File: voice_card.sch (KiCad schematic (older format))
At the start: 207 parts, among them J1 PCI_11_49, Q1 MMBF4391LT1G, Q10 DMMT3906, Q11 BC857BS, Q2 2N3904, Q3 BCM847, Q4 DMMT3904, Q5 DMMT3906, Q6 MMBF4391LT1G, Q7 BCM847, Q8 2N3904, Q9 DMMT3904, U1 TL074-, U10 TL072-, U11 TL074-, U12 NE555, U13 LM311M, U14 CD4052, U15 TL072-, U16 TL072-, U17 LM13700, U18 LM13700, U19 LM13700, U2 TL074-, U20 TL072-, U3 NE555, U4 LF351, U5 TL072-, U6 LM311M, U7 CD4052, U8 TL074-, U9 LF351

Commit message: DDR3 DIMM schematic symbol created, now assigning ins and outs to DIMM pins. Tedious
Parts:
- removed J1: PCI_11_49, MyModules:PCI-49-11-CARD-EDGE, symbol PCI_11_49
- added J1: DDR3-DIMM, MyModules:DDR3-DIMM-MO-269, symbol DDR3-DIMM
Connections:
- wire segments 691 -> 891
- no-connect marks 8 -> 9

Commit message: DDR3 DIMM connector switched over from PCI in board and schematic. Routing power traces now
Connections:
- wire segments 891 -> 655
- no-connect marks 9 -> 19

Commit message: power routed, now stitching grounds
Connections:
- net +12V: now also J1.192, J1.210, J1.217, J1.238
- net -12V: now also J1.184, J1.197, J1.221
- net GND: now also J1.114, J1.116, J1.117, J1.119, J1.12, J1.127, J1.128, J1.129, J1.135, J1.14, J1.160, J1.177, J1.178, J1.179, J1.187, J1.188, J1.195, J1.203, J1.204, J1.228, J1.229, J1.239, J1.240
- no-connect marks 19 -> 14

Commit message: stitching ground plane
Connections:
- net GND: now also J1.102, J1.103, J1.151, J1.152, J1.219, J1.52, J1.53, J1.59, J1.66, J1.70
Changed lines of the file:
@@
+	1    0    0    -1
+$EndComp
+$Comp
+L GND_E #PWR0184
+U 1 1 5660624A
+P 4950 18800
+F 0 "#PWR0184" V 4950 18800 30  0001 C CNN
+F 1 "GND_E" H 4950 18730 30  0001 C CNN
+F 2 "" H 4950 18800 60  0000 C CNN
+F 3 "" H 4950 18800 60  0000 C CNN
+	1    4950 18800
+	1    0    0    -1
+$EndComp
+$Comp
+L GND_E #PWR0185
+U 1 1 5660A47B
+P 5675 30000
+F 0 "#PWR0185" V 5675 30000 30  0001 C CNN
+F 1 "GND_E" H 5675 29930 30  0001 C CNN
+F 2 "" H 5675 30000 60  0000 C CNN
+F 3 "" H 5675 30000 60  0000 C CNN
+	1    5675 30000
 	1    0    0    -1
 $EndComp
@@
 	36100 8075 35700 8075
 Wire Wire Line
-	35700 8075 35700 9550
+	35700 9550 35700 8075
 Wire Wire Line
 	36700 8850 36800 8850
@@
 	30800 9700 36100 9700
 Wire Wire Line
-	35700 9550 35250 9550
+	35250 9550 35700 9550
 Wire Wire Line
 	35550 7750 35550 8575
@@
 	32450 5650 32600 5650
 Wire Wire Line
-	32600 5650 32600 4450
-Wire Wire Line
-	32600 4450 29700 4450
+	32600 4450 32600 5650
+Wire Wire Line
+	29700 4450 32600 4450
 Wire Wire Line
 	29700 4450 29700 4500
@@
 	35700 16875 35300 16875
 Wire Wire Line
-	35300 16875 35300 17375
+	35300 17375 35300 16875
 Wire Wire Line
 	36300 17275 36400 17275
@@
 	30400 17875 35700 17875
 Wire Wire Line
-	35300 17375 34850 17375
+	34850 17375 35300 17375
 Wire Wire Line
 	35150 15550 35150 16325
@@
 	32050 13450 32200 13450
 Wire Wire Line
-	32200 13450 32200 12250
-Wire Wire Line
-	32200 12250 29300 12250
+	32200 12250 32200 13450
+Wire Wire Line
+	29300 12250 32200 12250
 Wire Wire Line
 	29300 12250 29300 12300
@@
 	4550 23750 5675 23750
 Connection ~ 5675 23750
+Wire Wire Line
+	4950 18550 4950 18800
+Wire Wire Line
+	4950 18550 4550 18550
+Wire Wire Line
+	4550 18650 4950 18650
+Connection ~ 4950 18650
+Wire Wire Line
+	4550 18750 4950 18750
+Connection ~ 4950 18750
+Wire Wire Line
+	5675 29750 5675 30000
+Wire Wire Line
+	5675 29750 4550 29750
+Wire Wire Line
+	4550 29850 5675 29850
+Connection ~ 5675 29850
+Wire Wire Line
+	3075 29750 3950 29750
+Connection ~ 3075 29550
 $Comp
-L GND_E #PWR0184
-U 1 1 5660624A
-P 4950 18800
-F 0 "#PWR0184" V 4950 18800 30  0001 C CNN
-F 1 "GND_E" H 4950 18730 30  0001 C CNN
-F 2 "" H 4950 18800 60  0000 C CNN
-F 3 "" H 4950 18800 60  0000 C CNN
-	1    4950 18800
+L GND_E #PWR0186
+U 1 1 5660CF32
+P 2825 28300
+F 0 "#PWR0186" V 2825 28300 30  0001 C CNN
+F 1 "GND_E" H 2825 28230 30  0001 C CNN
+F 2 "" H 2825 28300 60  0000 C CNN
+F 3 "" H 2825 28300 60  0000 C CNN
+	1    2825 28300
+	-1   0    0    -1
+$EndComp
+Wire Wire Line
+	2825 28050 2825 28300
+$Comp
+L GND_E #PWR0187
+U 1 1 5660D926
+P 2825 24700
+F 0 "#PWR0187" V 2825 24700 30  0001 C CNN
+F 1 "GND_E" H 2825 24630 30  0001 C CNN
+F 2 "" H 2825 24700 60  0000 C CNN
+F 3 "" H 2825 24700 60  0000 C CNN
+	1    2825 24700
+	-1   0    0    -1
+$EndComp
+Wire Wire Line
+	2825 24450 2825 24700
+Wire Wire Line
+	2825 24450 3950 24450
+$Comp
+L GND_E #PWR0188
+U 1 1 5660E6B9
+P 2825 24000
+F 0 "#PWR0188" V 2825 24000 30  0001 C CNN
+F 1 "GND_E" H 2825 23930 30  0001 C CNN
+F 2 "" H 2825 24000 60  0000 C CNN
+F 3 "" H 2825 24000 60  0000 C CNN
+	1    2825 24000
+	-1   0    0    -1
+$EndComp
+Wire Wire Line
+	2825 23750 2825 24000
+Wire Wire Line
+	2825 23750 3950 23750
+$Comp
+L GND_E #PWR0189
+U 1 1 5660EC2D
+P 2825 25100
+F 0 "#PWR0189" V 2825 25100 30  0001 C CNN
+F 1 "GND_E" H 2825 25030 30  0001 C CNN
+F 2 "" H 2825 25100 60  0000 C CNN
+F 3 "" H 2825 25100 60  0000 C CNN
+	1    2825 25100
+	-1   0    0    -1
+$EndComp
+Wire Wire Line
+	2825 24850 2825 25100
+Wire Wire Line
+	2825 24850 3950 24850
+Wire Wire Line
+	2825 23050 3950 23050
+Wire Wire Line
+	3950 23150 2825 23150
+Connection ~ 2825 23150
+$Comp
+L GND_E #PWR0190
+U 1 1 5660FCD3
+P 2825 23300
+F 0 "#PWR0190" V 2825 23300 30  0001 C CNN
+F 1 "GND_E" H 2825 23230 30  0001 C CNN
+F 2 "" H 2825 23300 60  0000 C CNN
+F 3 "" H 2825 23300 60  0000 C CNN
+	1    2825 23300
+	-1   0    0    -1
+$EndComp
+Wire Wire Line
+	2825 23050 2825 23300
+Wire Wire Line
+	5050 20950 4550 20950
+Wire Wire Line
+	4550 21050 5050 21050
+Connection ~ 5050 21050
+$Comp
+L GND_E #PWR0191
+U 1 1 566108F5
+P 5050 21200
+F 0 "#PWR0191" V 5050 21200 30  0001 C CNN
+F 1 "GND_E" H 5050 21130 30  0001 C CNN
+F 2 "" H 5050 21200 60  0000 C CNN
+F 3 "" H 5050 21200 60  0000 C CNN
+	1    5050 21200
 	1    0    0    -1
 $EndComp
 Wire Wire Line
-	4950 18550 4950 18800
-Wire Wire Line
-	4950 18550 4550 18550
-Wire Wire Line
-	4550 18650 4950 18650
-Connection ~ 4950 18650
-Wire Wire Line
-	4550 18750 4950 18750
-Connection ~ 4950 18750
+	5050 20950 5050 21200
 $Comp
 L GND_E #PWR?
-U 1 1 5660A47B
-P 5675 30000
-F 0 "#PWR?" V 5675 30000 30  0001 C CNN
-F 1 "GND_E" H 5675 29930 30  0001 C CNN
-F 2 "" H 5675 30000 60  0000 C CNN
-F 3 "" H 5675 30000 60  0000 C CNN
-	1    5675 30000
+U 1 1 5661486B
+P 5675 28000
+F 0 "#PWR?" V 5675 28000 30  0001 C CNN
+F 1 "GND_E" H 5675 27930 30  0001 C CNN
+F 2 "" H 5675 28000 60  0000 C CNN
+F 3 "" H 5675 28000 60  0000 C CNN
+	1    5675 28000
 	1    0    0    -1
 $EndComp
 Wire Wire Line
-	5675 29750 5675 30000
-Wire Wire Line
-	5675 29750 4550 29750
-Wire Wire Line
-	4550 29850 5675 29850
-Connection ~ 5675 29850
-Wire Wire Line
-	3075 29750 3950 29750
-Connection ~ 3075 29550
+	5675 27750 5675 28000
+Wire Wire Line
+	5675 27750 4550 27750
 $EndSCHEMATC

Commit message: decoupling caps placed and routed. Still stitching ground plane
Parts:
- added C35, C36, C37, C38, C39, C40: 100n, MyModules:SM0603-C-JRL, symbol C_US
- TP1, TP8: footprint MyModules:TEST_POINT_5000_SERIES -> MyModules:TEST_PAD
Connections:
- net +12V: now also C35.1, C37.1, C39.1
- net -12V: now also C36.2, C38.2, C40.2
- net GND: now also J1.164, J1.78, C35.2, C36.1, C37.2, C38.1, C39.2, C40.1

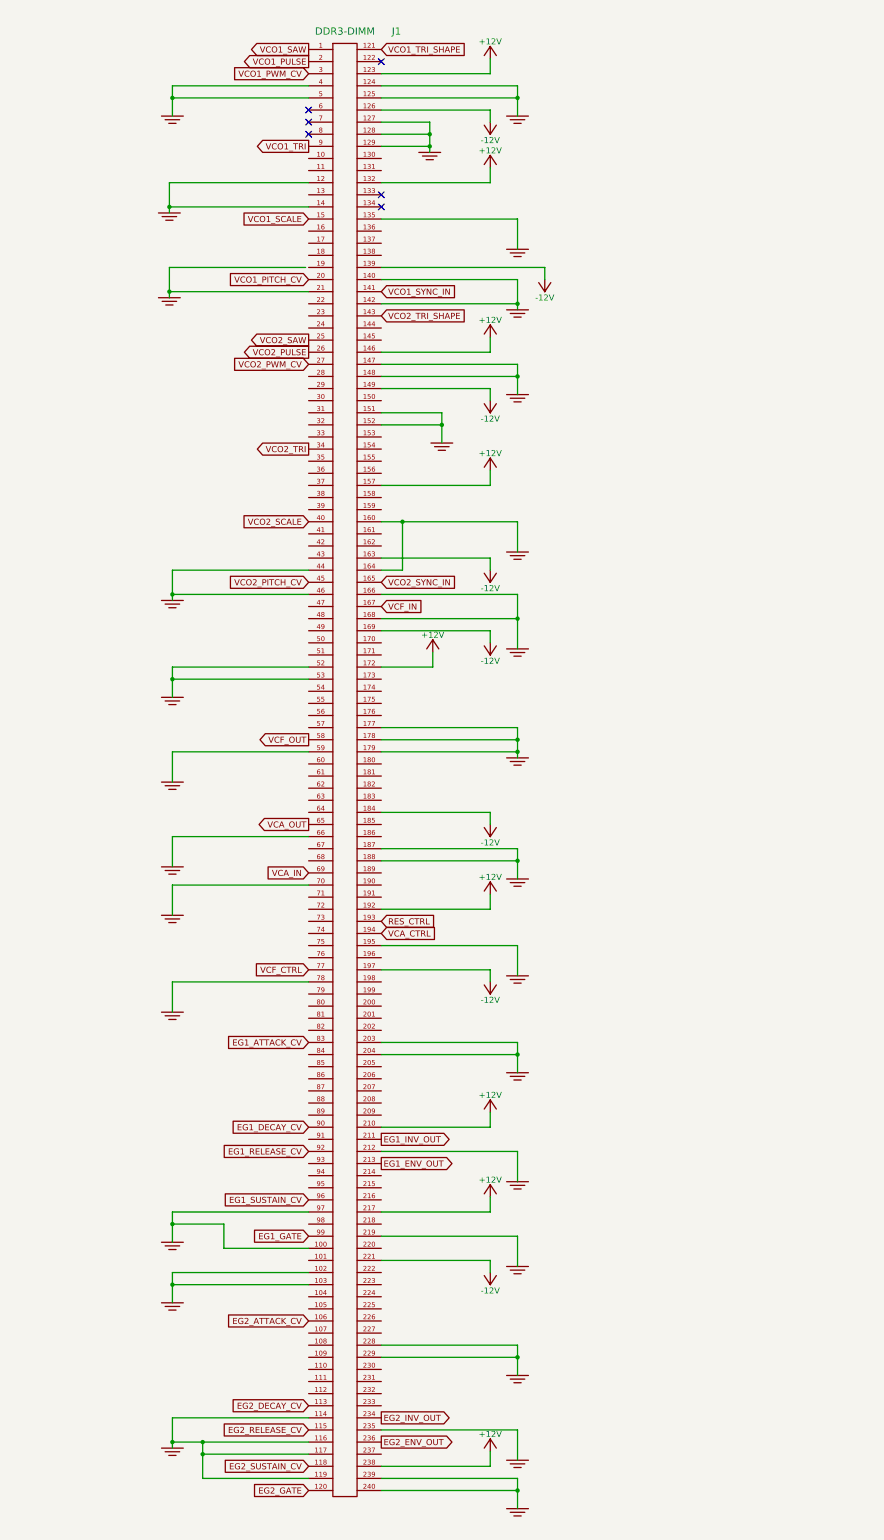
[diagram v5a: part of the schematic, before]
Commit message: placed silkscreen component references. still need to finish up ground stitching
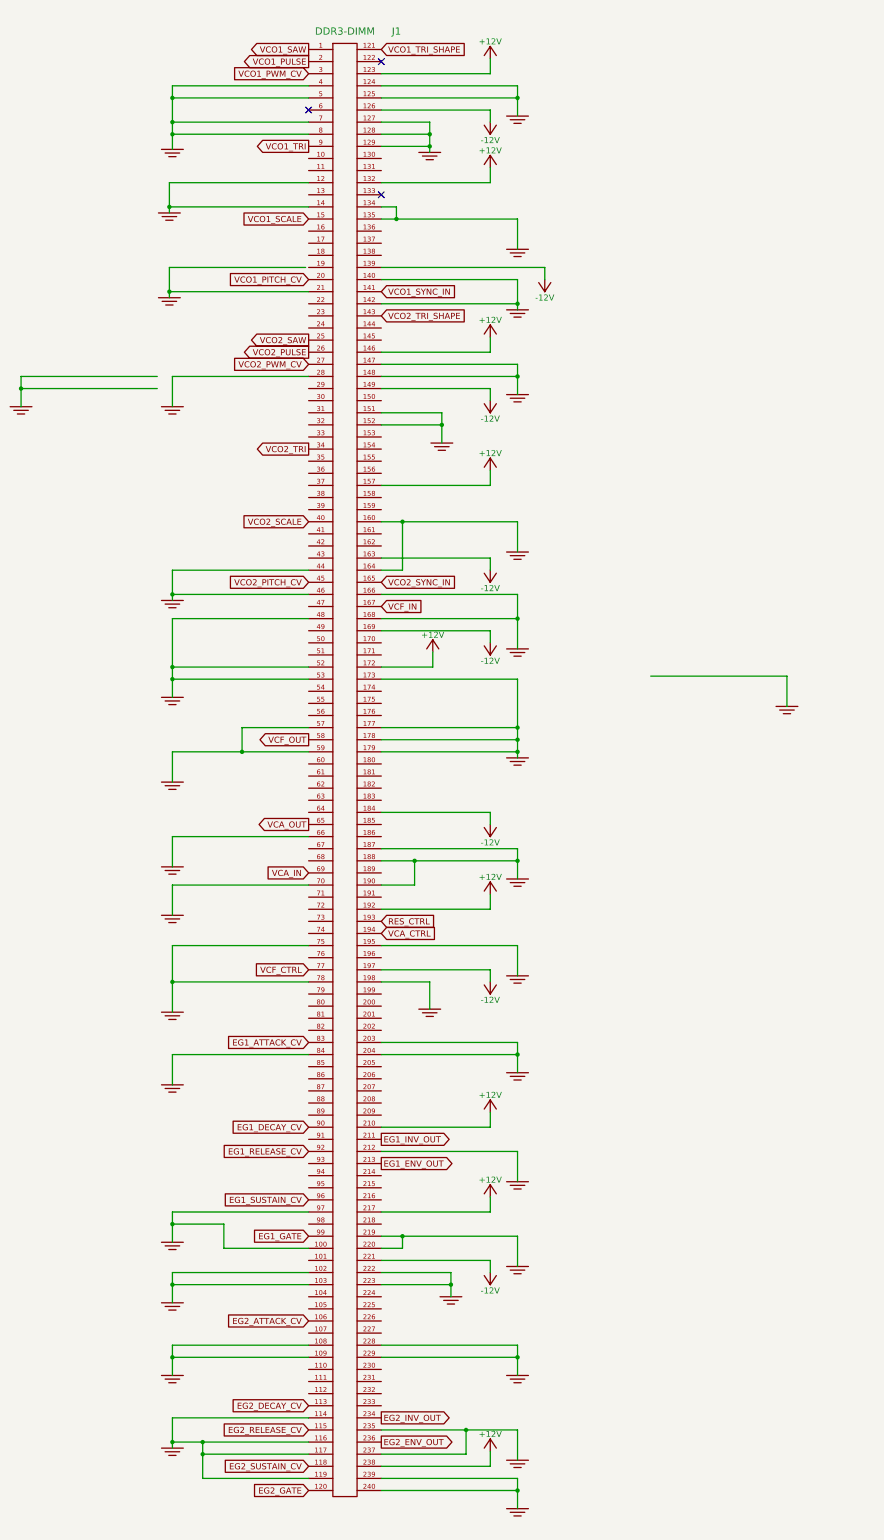
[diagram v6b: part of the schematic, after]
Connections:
- net GND: now also J1.108, J1.109, J1.134, J1.173, J1.190, J1.198, J1.220, J1.222, J1.223, J1.237, J1.28, J1.48, J1.57, J1.7, J1.75, J1.8, J1.84
- no-connect marks 14 -> 11

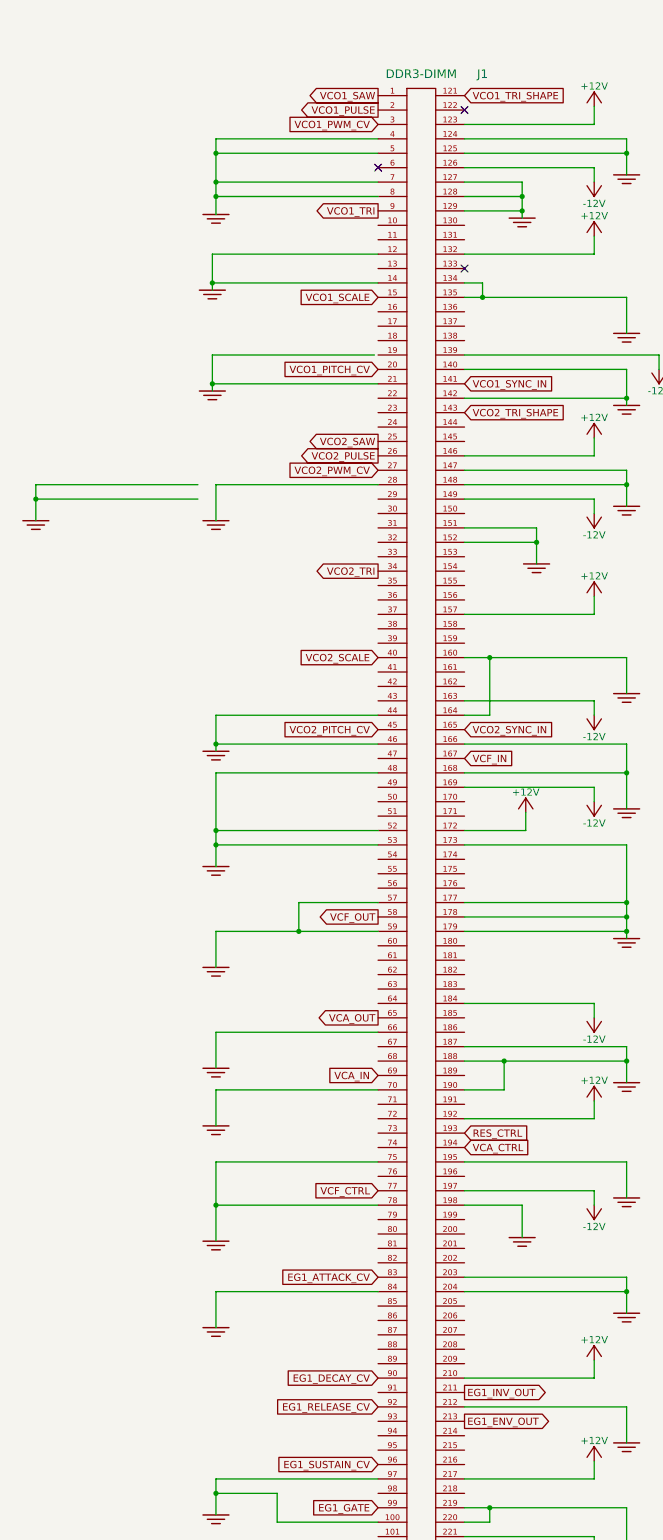
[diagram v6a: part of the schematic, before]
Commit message: stitching done. 21 unconnected, all of which should be resolved by connecting pins on J1
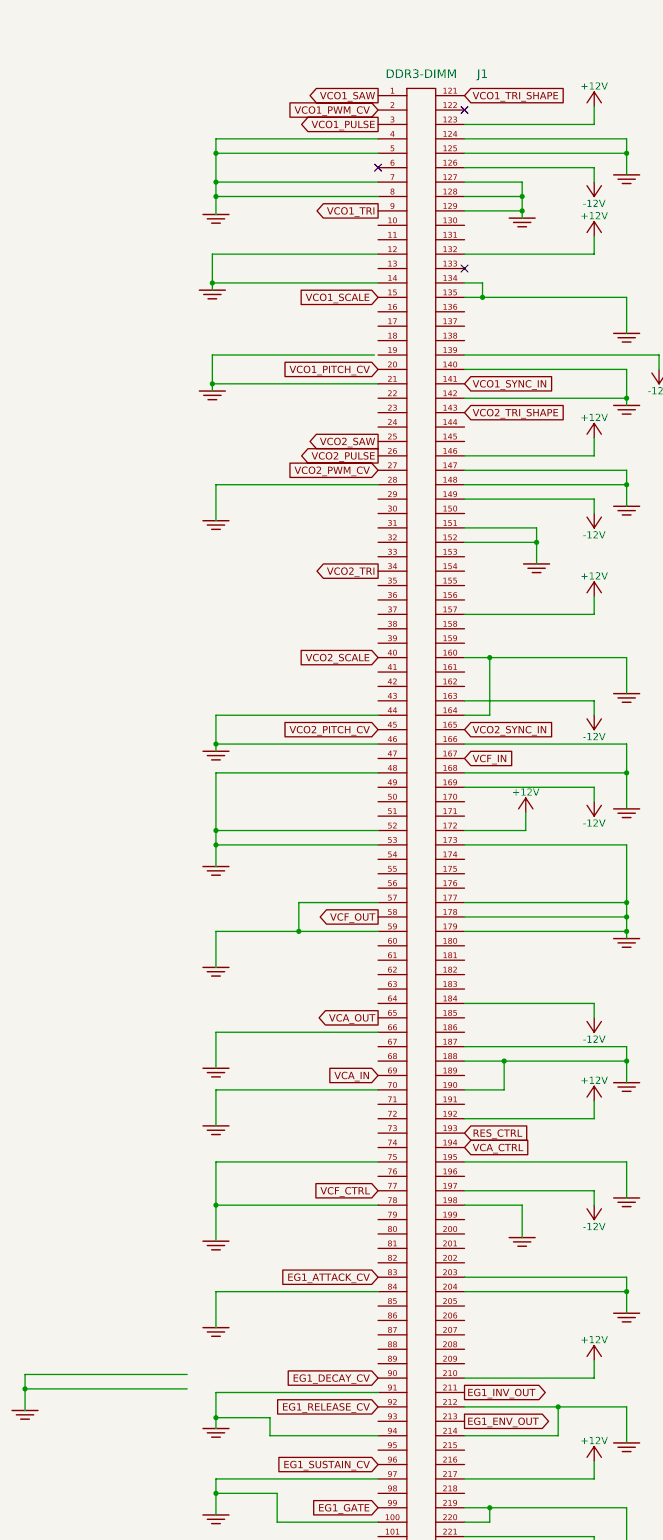
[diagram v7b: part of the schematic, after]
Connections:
- net GND: now also J1.214, J1.91, J1.94
- net VCO1_PULSE: now also J1.3; no longer J1.2
- net VCO1_PWM_CV: now also J1.2; no longer J1.3
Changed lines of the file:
@@
 Comment4 ""
 $EndDescr
-Text GLabel 3950 18150 0    50   Input ~ 0
+Text GLabel 3950 18050 0    50   Input ~ 0
 VCO1_PWM_CV
 Text GLabel 4550 19950 2    50   Input ~ 0
 VCO1_SYNC_IN
-Text GLabel 3950 18050 0    50   Output ~ 0
+Text GLabel 3950 18150 0    50   Output ~ 0
 VCO1_PULSE
 Text GLabel 3950 17950 0    50   Output ~ 0
@@
 $EndComp
 $Comp
-L GND_E #PWR?
+L GND_E #PWR0206
 U 1 1 56624D56
 P 7900 23375
-F 0 "#PWR?" V 7900 23375 30  0001 C CNN
+F 0 "#PWR0206" V 7900 23375 30  0001 C CNN
 F 1 "GND_E" H 7900 23305 30  0001 C CNN
 F 2 "" H 7900 23375 60  0000 C CNN
@@
 $EndComp
 $Comp
-L GND_E #PWR?
+L GND_E #PWR0207
 U 1 1 56627D89
 P 2825 28900
-F 0 "#PWR?" V 2825 28900 30  0001 C CNN
+F 0 "#PWR0207" V 2825 28900 30  0001 C CNN
 F 1 "GND_E" H 2825 28830 30  0001 C CNN
 F 2 "" H 2825 28900 60  0000 C CNN
@@
 $EndComp
 $Comp
-L GND_E #PWR?
+L GND_E #PWR0208
 U 1 1 56628E3F
 P 5125 28250
-F 0 "#PWR?" V 5125 28250 30  0001 C CNN
+F 0 "#PWR0208" V 5125 28250 30  0001 C CNN
 F 1 "GND_E" H 5125 28180 30  0001 C CNN
 F 2 "" H 5125 28250 60  0000 C CNN
@@
 $EndComp
 $Comp
-L GND_E #PWR?
+L GND_E #PWR0209
 U 1 1 5662AB37
 P 2825 26500
-F 0 "#PWR?" V 2825 26500 30  0001 C CNN
+F 0 "#PWR0209" V 2825 26500 30  0001 C CNN
 F 1 "GND_E" H 2825 26430 30  0001 C CNN
 F 2 "" H 2825 26500 60  0000 C CNN
@@
 $EndComp
 $Comp
-L GND_E #PWR?
+L GND_E #PWR0210
 U 1 1 5662B483
 P 4950 25875
-F 0 "#PWR?" V 4950 25875 30  0001 C CNN
+F 0 "#PWR0210" V 4950 25875 30  0001 C CNN
 F 1 "GND_E" H 4950 25805 30  0001 C CNN
 F 2 "" H 4950 25875 60  0000 C CNN
@@
 $EndComp
 $Comp
-L GND_E #PWR?
+L GND_E #PWR0211
 U 1 1 56632199
-P 1575 20900
-F 0 "#PWR?" V 1575 20900 30  0001 C CNN
-F 1 "GND_E" H 1575 20830 30  0001 C CNN
-F 2 "" H 1575 20900 60  0000 C CNN
-F 3 "" H 1575 20900 60  0000 C CNN
-	1    1575 20900
+P 1500 27075
+F 0 "#PWR0211" V 1500 27075 30  0001 C CNN
+F 1 "GND_E" H 1500 27005 30  0001 C CNN
+F 2 "" H 1500 27075 60  0000 C CNN
+F 3 "" H 1500 27075 60  0000 C CNN
+	1    1500 27075
 	-1   0    0    -1
 $EndComp
 $Comp
-L GND_E #PWR?
+L GND_E #PWR0212
 U 1 1 566339B2
 P 2825 20900
-F 0 "#PWR?" V 2825 20900 30  0001 C CNN
+F 0 "#PWR0212" V 2825 20900 30  0001 C CNN
 F 1 "GND_E" H 2825 20830 30  0001 C CNN
 F 2 "" H 2825 20900 60  0000 C CNN
@@
 Connection ~ 2825 23050
 Wire Wire Line
-	1575 20650 2700 20650
+	1500 26825 2625 26825
 Wire Wire Line
-	2700 20750 1575 20750
-Connection ~ 1575 20750
+	2625 26925 1500 26925
+Connection ~ 1500 26925
 Wire Wire Line
-	1575 20650 1575 20900
+	1500 26825 1500 27075
 Wire Wire Line
 	2825 20650 2825 20900
@@
 	3950 18550 2825 18550
 Connection ~ 2825 18550
+$Comp
+L GND_E #PWR?
+U 1 1 5664285F
+P 2825 27200
+F 0 "#PWR?" V 2825 27200 30  0001 C CNN
+F 1 "GND_E" H 2825 27130 30  0001 C CNN
+F 2 "" H 2825 27200 60  0000 C CNN
+F 3 "" H 2825 27200 60  0000 C CNN
+	1    2825 27200
+	-1   0    0    -1
+$EndComp
+Wire Wire Line
+	2825 26950 2825 27200
+Wire Wire Line
+	2825 26950 3950 26950
+Wire Wire Line
+	3950 27250 3200 27250
+Wire Wire Line
+	3200 27250 3200 27125
+Wire Wire Line
+	3200 27125 2825 27125
+Connection ~ 2825 27125
+Wire Wire Line
+	4550 27250 5200 27250
+Wire Wire Line
+	5200 27250 5200 27050
+Connection ~ 5200 27050
 $EndSCHEMATC
